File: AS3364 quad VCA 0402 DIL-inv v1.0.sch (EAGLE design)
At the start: 44 parts, among them IC1 TL072JD, IC2 TL072JD

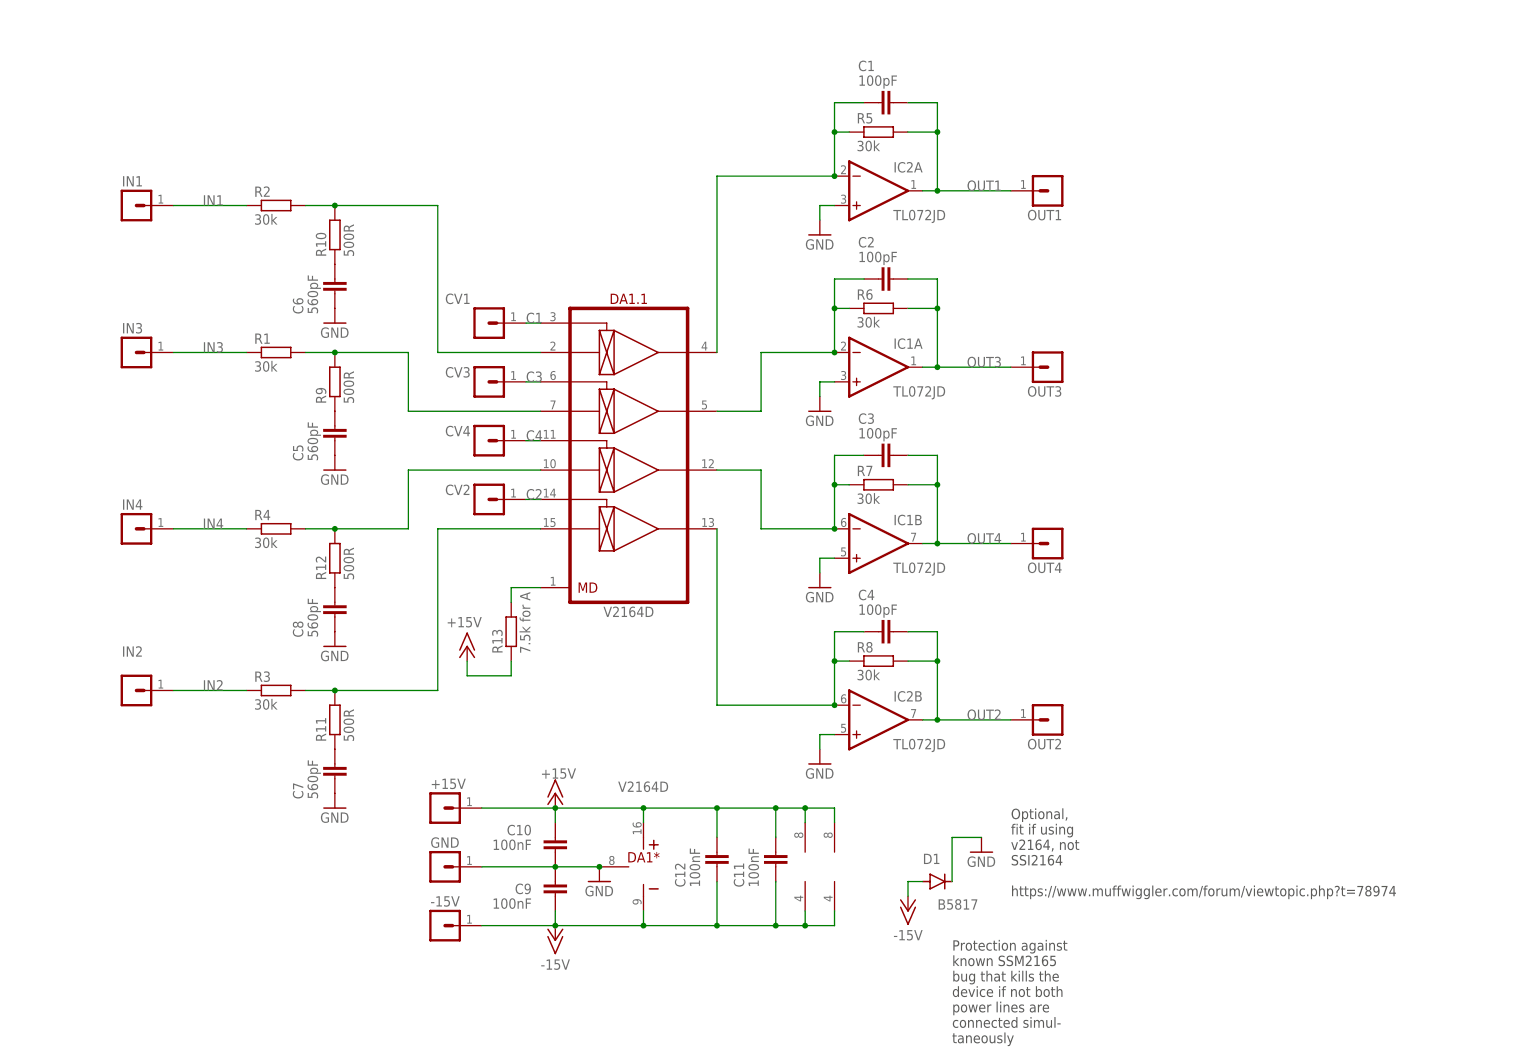
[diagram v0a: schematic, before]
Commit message: Added AS3364 versions of quad VCA
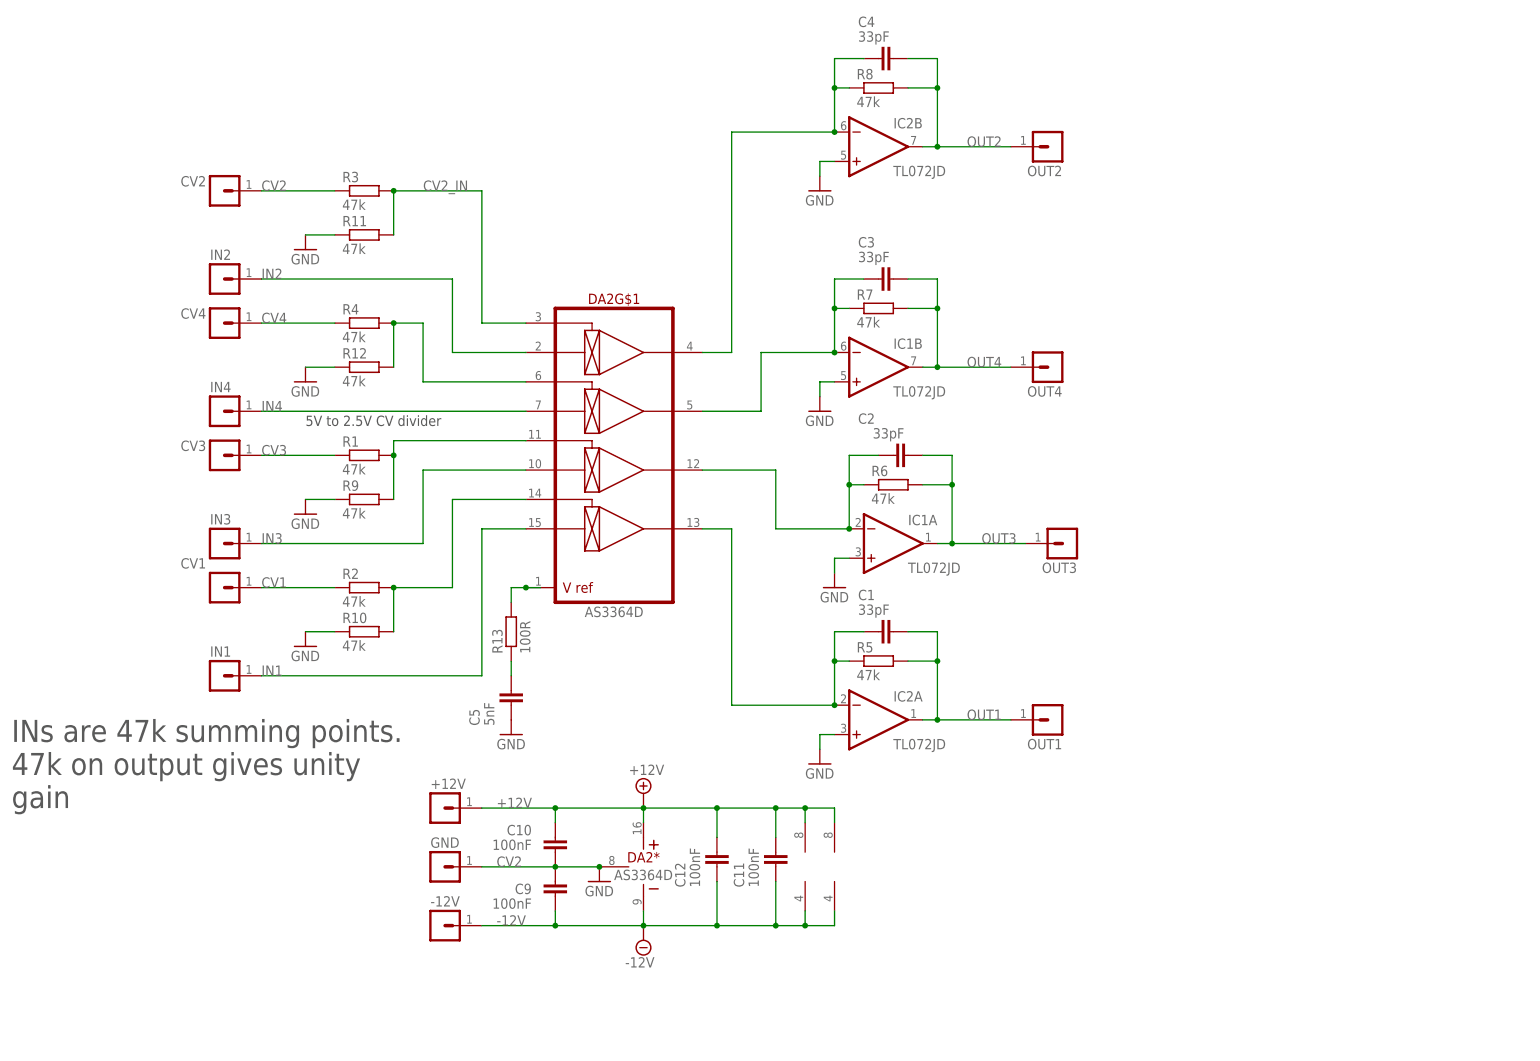
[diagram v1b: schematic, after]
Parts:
- removed C6, C7, C8: 560pF, rcl:C-EUC0603
- removed D1: B5817, diode:DIODE-SOD323-R
- removed DA1: V2164D, ic-coolaudio:V2164D
- added DA2: AS3364D, joakim:AS3364D
- C1, C2, C3, C4: value 100pF -> 33pF
- C5: value 560pF -> 5nF; device rcl:C-EUC0603 -> rcl:C-EUC0402
- R1, R2, R3, R4, R5, R6, R7, R8: value 30k -> 47k
- R10, R11, R12, R9: value 500R -> 47k
- R13: value 7.5k for A -> 100R
- renumbered +15V to +12V, -15V to -12V
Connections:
- removed net +15V: +12V.1, C10.2, C11.2, C12.2, DA1*.V+, IC1P.V+, IC2P.V+, R13.1
- removed net -15V: -12V.1, C11.1, C12.1, C9.1, D1.A, DA1*.V-, IC1P.V-, IC2P.V-
- removed net C1: CV1.1, DA1.1.CV1
- removed net C2: CV2.1, DA1.1.CV4
- removed net C3: CV3.1, DA1.1.CV2
- removed net C4: CV4.1, DA1.1.CV3
- removed net N$11: C7.2, R11.1
- removed net N$17: DA1.1.IN2, R1.2, R9.2
- removed net N$18: DA1.1.IN1, R10.2, R2.2
- removed net N$19: DA1.1.IN4, R11.2, R3.2
- removed net N$20: DA1.1.IN3, R12.2, R4.2
- removed net N$9: C5.2, R9.1
- new net +12V: +12V.1, C10.2, C11.2, C12.2, DA2*.V+, IC1P.V+, IC2P.V+
- new net -12V: -12V.1, C11.1, C12.1, C9.1, DA2*.V-, IC1P.V-, IC2P.V-
- new net CV1: CV1.1, R2.1
- new net CV2: CV2.1, R3.1
- new net CV2_IN: DA2G$1.CV1, R11.2, R3.2
- new net CV3: CV3.1, R1.1
- new net CV4: CV4.1, R4.1
- new net N$14: C5.2, R13.1
- new net N$21: DA2G$1.CV4, R10.2, R2.2
- net GND: now also DA2*.GND, R10.1, R11.1, R12.1, R9.1; no longer C6.1, C7.1, C8.1, D1.C, DA1*.GND
- net IN1: now also DA2G$1.IN4; no longer R2.1
- net IN2: now also DA2G$1.IN1; no longer R3.1
- net IN3: now also DA2G$1.IN3; no longer R1.1
- net IN4: now also DA2G$1.IN2; no longer R4.1
- net N$1: now also DA2G$1.OUT1; no longer DA1.1.OUT4
- net N$10: now also DA2G$1.CV2, R12.2, R4.2; no longer C6.2, R10.1
- net N$12: now also DA2G$1.CV3, R1.2, R9.2; no longer C8.2, R12.1
- net N$2: now also DA2G$1.VREF; no longer DA1.1.MD
- net N$3: now also DA2G$1.OUT2; no longer DA1.1.OUT3
- net N$5: now also DA2G$1.OUT3; no longer DA1.1.OUT2
- net N$7: now also DA2G$1.OUT4; no longer DA1.1.OUT1
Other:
- note added: "5V to 2.5V CV divider"
- note added: "INs are 47k summing points. 47k on output gives unity gain"
- note removed: "Optional, fit if using v2164, not SSI2164 https://www.muffwiggler.com/forum/viewtopic.php?t=78974"
- note removed: "Protection against known SSM2165 bug that kills the device if not both power lines are connected simul- taneously"
- moved on the sheet: C1, C2, C3, C4, C5, CV1, CV2, CV3, CV4, IC1A, IC1B, IC2A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

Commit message: Checked most things, changed CV input resistors, added cap to mixer output
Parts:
- R1, R2, R3, R4: value 47k -> 33k
- R10, R11, R12, R9: value 47k -> 22k
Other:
- note added: "5V to 2V CV divider"
- note removed: "5V to 2.5V CV divider"
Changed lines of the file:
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@@
 <part name="C3" library="rcl" library_urn="urn:adsk.eagle:library:334" deviceset="C-EU" device="C0402" package3d_urn="urn:adsk.eagle:package:23626/2" value="33pF"/>
 <part name="C4" library="rcl" library_urn="urn:adsk.eagle:library:334" deviceset="C-EU" device="C0402" package3d_urn="urn:adsk.eagle:package:23626/2" value="33pF"/>
-<part name="R1" library="rcl" library_urn="urn:adsk.eagle:library:334" deviceset="R-EU_" device="R0402" package3d_urn="urn:adsk.eagle:package:23547/3" value="47k"/>
-<part name="R2" library="rcl" library_urn="urn:adsk.eagle:library:334" deviceset="R-EU_" device="R0402" package3d_urn="urn:adsk.eagle:package:23547/3" value="47k"/>
-<part name="R3" library="rcl" library_urn="urn:adsk.eagle:library:334" deviceset="R-EU_" device="R0402" package3d_urn="urn:adsk.eagle:package:23547/3" value="47k"/>
-<part name="R4" library="rcl" library_urn="urn:adsk.eagle:library:334" deviceset="R-EU_" device="R0402" package3d_urn="urn:adsk.eagle:package:23547/3" value="47k"/>
+<part name="R1" library="rcl" library_urn="urn:adsk.eagle:library:334" deviceset="R-EU_" device="R0402" package3d_urn="urn:adsk.eagle:package:23547/3" value="33k"/>
+<part name="R2" library="rcl" library_urn="urn:adsk.eagle:library:334" deviceset="R-EU_" device="R0402" package3d_urn="urn:adsk.eagle:package:23547/3" value="33k"/>
+<part name="R3" library="rcl" library_urn="urn:adsk.eagle:library:334" deviceset="R-EU_" device="R0402" package3d_urn="urn:adsk.eagle:package:23547/3" value="33k"/>
+<part name="R4" library="rcl" library_urn="urn:adsk.eagle:library:334" deviceset="R-EU_" device="R0402" package3d_urn="urn:adsk.eagle:package:23547/3" value="33k"/>
 <part name="R5" library="rcl" library_urn="urn:adsk.eagle:library:334" deviceset="R-EU_" device="R0402" package3d_urn="urn:adsk.eagle:package:23547/3" value="47k"/>
 <part name="R6" library="rcl" library_urn="urn:adsk.eagle:library:334" deviceset="R-EU_" device="R0402" package3d_urn="urn:adsk.eagle:package:23547/3" value="47k"/>
 <part name="R7" library="rcl" library_urn="urn:adsk.eagle:library:334" deviceset="R-EU_" device="R0402" package3d_urn="urn:adsk.eagle:package:23547/3" value="47k"/>
 <part name="R8" library="rcl" library_urn="urn:adsk.eagle:library:334" deviceset="R-EU_" device="R0402" package3d_urn="urn:adsk.eagle:package:23547/3" value="47k"/>
-<part name="R9" library="rcl" library_urn="urn:adsk.eagle:library:334" deviceset="R-EU_" device="R0402" package3d_urn="urn:adsk.eagle:package:23547/3" value="47k"/>
-<part name="R10" library="rcl" library_urn="urn:adsk.eagle:library:334" deviceset="R-EU_" device="R0402" package3d_urn="urn:adsk.eagle:package:23547/3" value="47k"/>
-<part name="R11" library="rcl" library_urn="urn:adsk.eagle:library:334" deviceset="R-EU_" device="R0402" package3d_urn="urn:adsk.eagle:package:23547/3" value="47k"/>
-<part name="R12" library="rcl" library_urn="urn:adsk.eagle:library:334" deviceset="R-EU_" device="R0402" package3d_urn="urn:adsk.eagle:package:23547/3" value="47k"/>
+<part name="R9" library="rcl" library_urn="urn:adsk.eagle:library:334" deviceset="R-EU_" device="R0402" package3d_urn="urn:adsk.eagle:package:23547/3" value="22k"/>
+<part name="R10" library="rcl" library_urn="urn:adsk.eagle:library:334" deviceset="R-EU_" device="R0402" package3d_urn="urn:adsk.eagle:package:23547/3" value="22k"/>
+<part name="R11" library="rcl" library_urn="urn:adsk.eagle:library:334" deviceset="R-EU_" device="R0402" package3d_urn="urn:adsk.eagle:package:23547/3" value="22k"/>
+<part name="R12" library="rcl" library_urn="urn:adsk.eagle:library:334" deviceset="R-EU_" device="R0402" package3d_urn="urn:adsk.eagle:package:23547/3" value="22k"/>
 <part name="C9" library="rcl" library_urn="urn:adsk.eagle:library:334" deviceset="C-EU" device="C0402" package3d_urn="urn:adsk.eagle:package:23626/2" value="100nF"/>
 <part name="C10" library="rcl" library_urn="urn:adsk.eagle:library:334" deviceset="C-EU" device="C0402" package3d_urn="urn:adsk.eagle:package:23626/2" value="100nF"/>
@@
 47k on output gives unity
 gain</text>
-<text x="5.08" y="58.42" size="1.778" layer="97">5V to 2.5V CV divider</text>
+<text x="5.08" y="58.42" size="1.778" layer="97">5V to 2V CV divider</text>
 </plain>
 <instances>
